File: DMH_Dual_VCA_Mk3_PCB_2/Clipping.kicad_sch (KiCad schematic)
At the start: 26 parts, among them SW1 SW_DPDT_OnOffOn_x2, U8 TL074

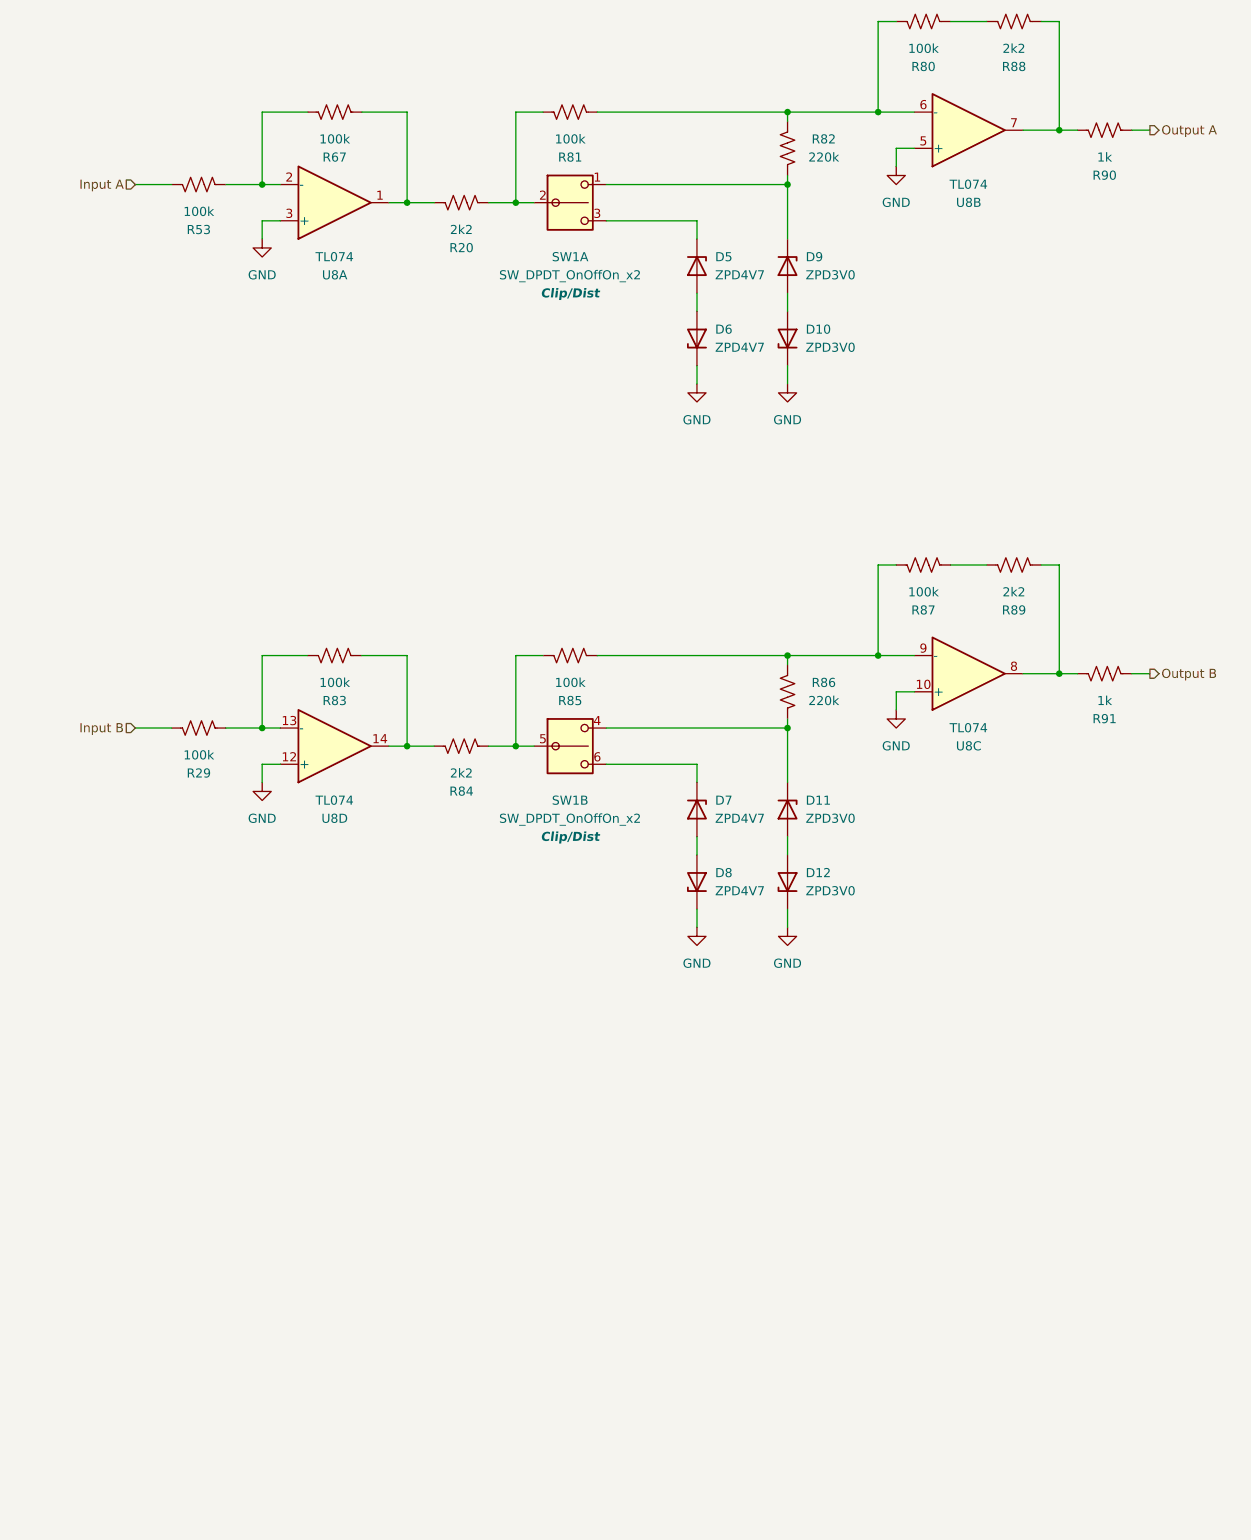
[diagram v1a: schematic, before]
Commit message: Added clipping LED to schematic
Still need to add to Panel
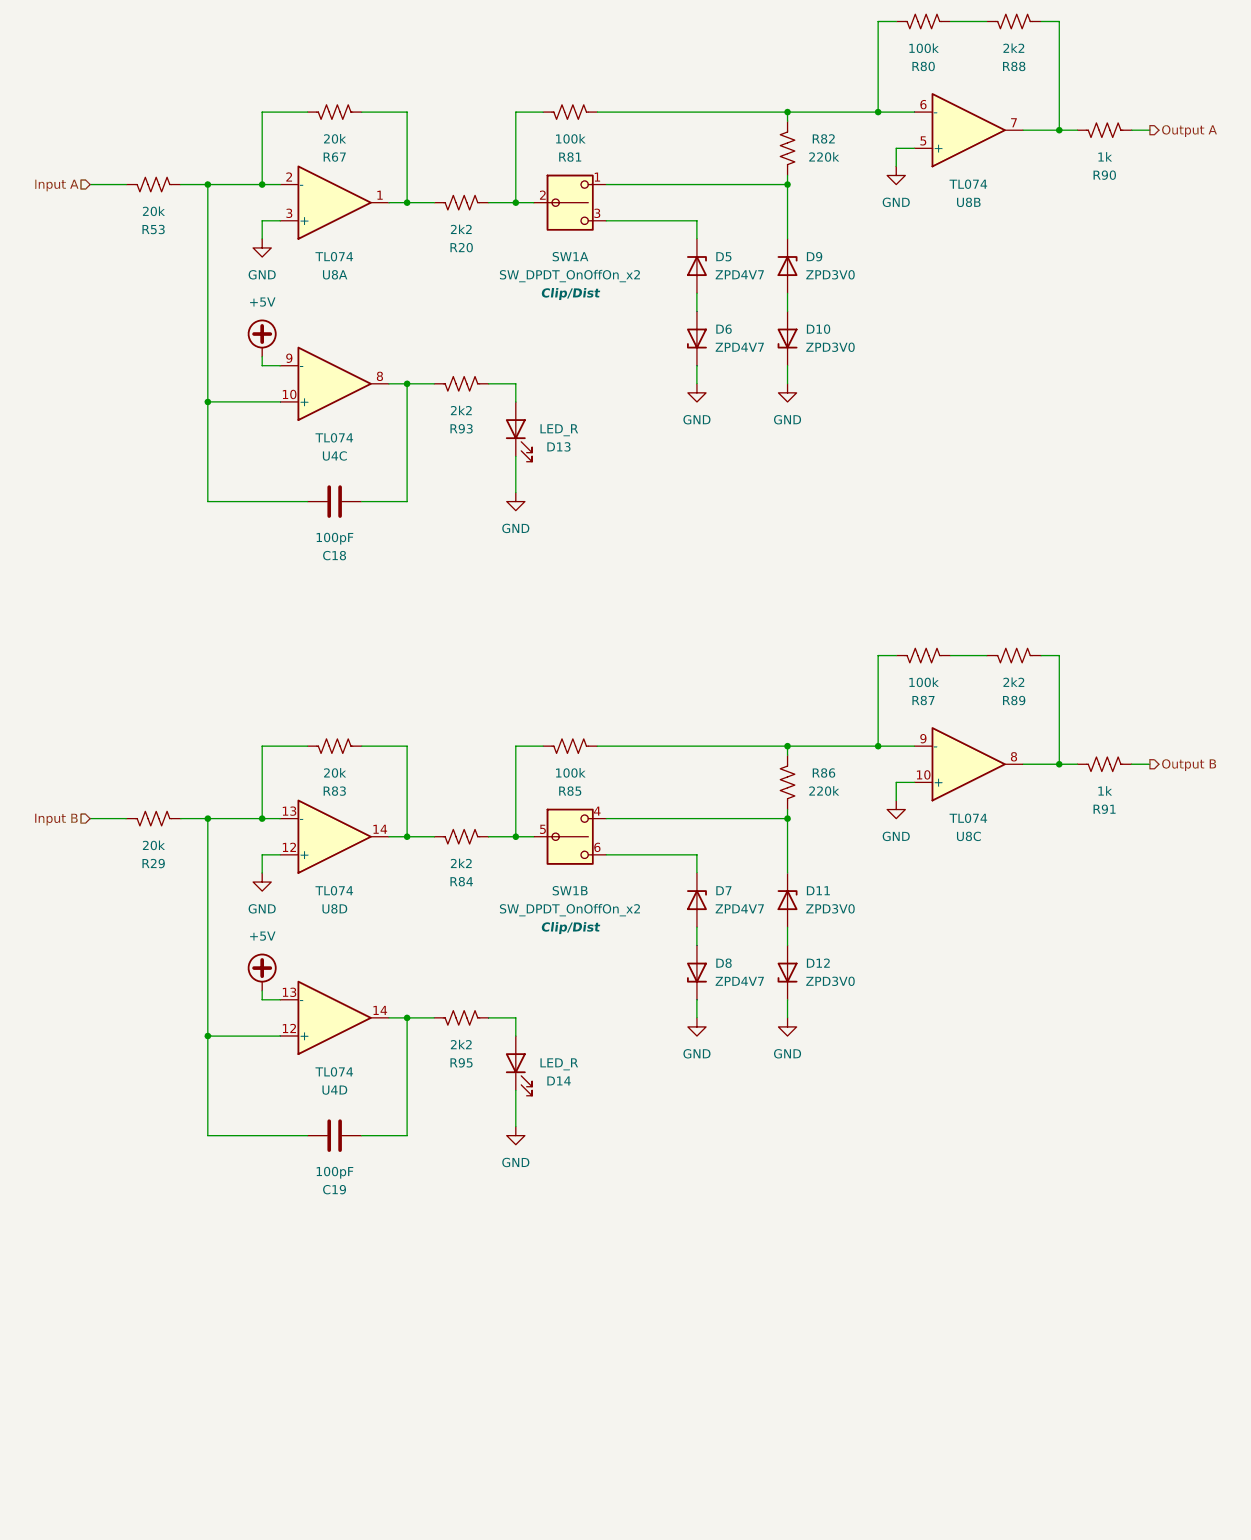
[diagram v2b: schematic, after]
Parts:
- added C18, C19: 100pF, Capacitor_THT:C_Disc_D3.0mm_W2.0mm_P2.50mm, symbol Device:C
- added D13, D14: LED_R, LED_THT:LED_D3.0mm, symbol Device:LED
- added R93, R95: 2k2, Resistor_THT:R_Axial_DIN0207_L6.3mm_D2.5mm_P7.62mm_Horizontal, symbol Device:R_US
- added U4: TL074, Package_DIP:DIP-14_W7.62mm_Socket, symbol Amplifier_Operational:TL074
- R29, R53, R67, R83: value 100k -> 20k
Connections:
- net GND: now also D13.1 (K), D14.1 (K)
- net at R53.2, R67.2, U8.2 (-): now also C18.1, U4.10 (+)
- net at R29.2, R83.2, U8.13 (-): now also C19.1, U4.12 (+)
- new net: D13.2 (A), R93.2
- new net: C18.2, R93.1, U4.8
- new net: C19.2, R95.1, U4.14
- new net: D14.2 (A), R95.2
- new net +5V: U4.13 (-), U4.9 (-)
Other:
- moved on the sheet: D11, D12, D7, D8, R29, R53, R83, R84, R85, R86, R87, R89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

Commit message: Improved clipping indication
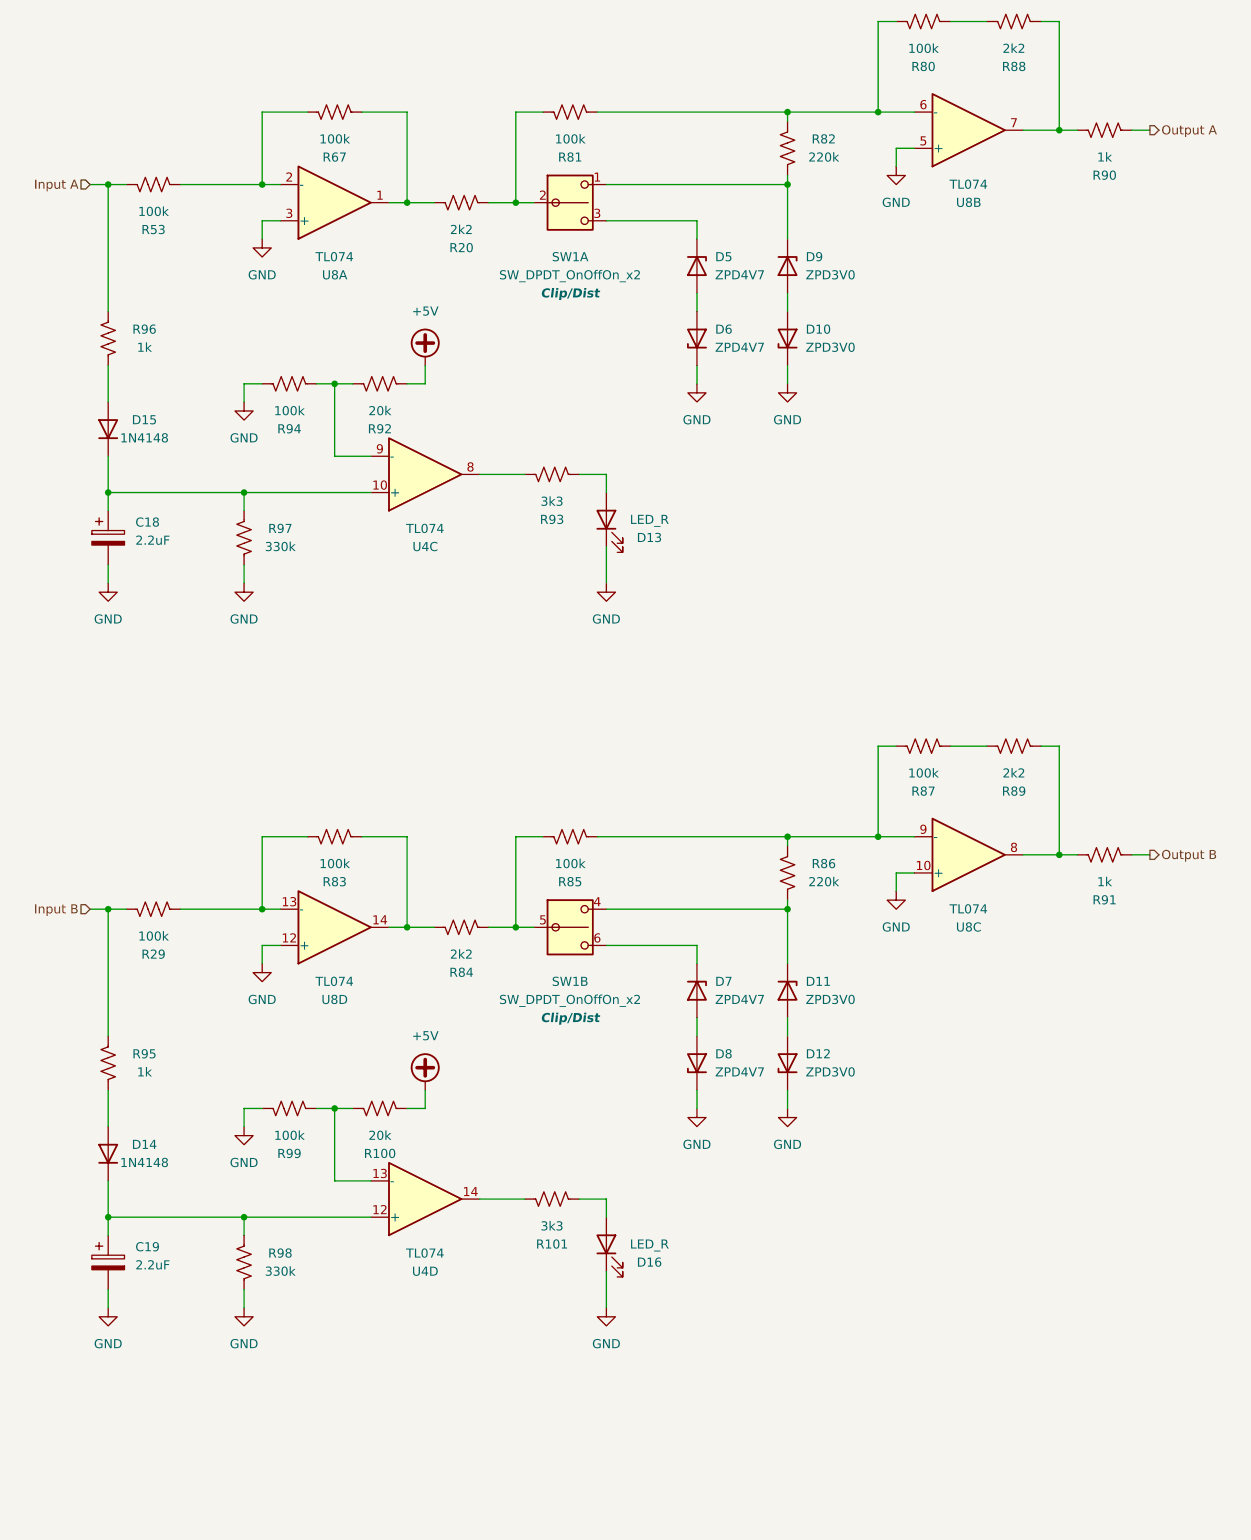
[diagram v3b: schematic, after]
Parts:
- removed C18, C19: 100pF, Capacitor_THT:C_Disc_D3.0mm_W2.0mm_P2.50mm, symbol Device:C
- removed D14: LED_R, LED_THT:LED_D3.0mm, symbol Device:LED
- added C18, C19: 2.2uF, Capacitor_THT:CP_Radial_D4.0mm_P1.50mm, symbol Device:C_Polarized
- added D14, D15: 1N4148, Diode_THT:D_DO-35_SOD27_P7.62mm_Horizontal, symbol Diode:1N4148
- added D16: LED_R, LED_THT:LED_D3.0mm, symbol Device:LED
- added R100, R92: 20k, Resistor_THT:R_Axial_DIN0207_L6.3mm_D2.5mm_P7.62mm_Horizontal, symbol Device:R_US
- added R101: 3k3, Resistor_THT:R_Axial_DIN0207_L6.3mm_D2.5mm_P7.62mm_Horizontal, symbol Device:R_US
- added R94, R99: 100k, Resistor_THT:R_Axial_DIN0207_L6.3mm_D2.5mm_P7.62mm_Horizontal, symbol Device:R_US
- added R96: 1k, Resistor_THT:R_Axial_DIN0207_L6.3mm_D2.5mm_P7.62mm_Horizontal, symbol Device:R_US
- added R97, R98: 330k, Resistor_THT:R_Axial_DIN0207_L6.3mm_D2.5mm_P7.62mm_Horizontal, symbol Device:R_US
- R29, R53, R67, R83: value 20k -> 100k
- R93: value 2k2 -> 3k3
- R95: value 2k2 -> 1k
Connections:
- net +5V: now also R100.2, R92.2; no longer U4.13 (-), U4.9 (-)
- net GND: now also C18.2, C19.2, D16.1 (K), R94.1, R97.1, R98.1, R99.1
- net Input A: now also R96.2
- net Input B: now also R95.2
- net at R53.2, R67.2, U8.2 (-): no longer U4.10 (+)
- net at U4.14: now also R101.1; no longer R95.1
- net at R29.2, R83.2, U8.13 (-): no longer U4.12 (+)
- new net: D15.2 (A), R96.1
- new net: C18.1, D15.1 (K), R97.2, U4.10 (+)
- new net: D16.2 (A), R101.2
- new net: C19.1, D14.1 (K), R98.2, U4.12 (+)
- new net: R100.1, R99.2, U4.13 (-)
- new net: R92.1, R94.2, U4.9 (-)
- new net: D14.2 (A), R95.1
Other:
- moved on the sheet: D11, D12, D13, D7, D8, R29, R83, R84, R85, R86, R87, R89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
